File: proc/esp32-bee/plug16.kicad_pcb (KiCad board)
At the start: 2 copper layers, 37 x 31.6 mm, 17 parts, among them J7 Moat_Bus_device, Q5 2N7002, U1 VXO78, U3 P82B96, U4 P82B96, U5 ESPBEE

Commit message: Fixup espbee
move driver ICs away from the antenna
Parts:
- moved REF** 9.04 mm to (54.6, 50.8)
- moved C5 2.54 mm to (57.8, 52.9)
- moved C7 2.54 mm to (53.8, 52.9)
- moved U3 2.54 mm to (55.9, 48.9)
- moved U4 2.54 mm to (55.9, 56.9)
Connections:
- J7 pad 15: (no net) -> /TXD2
- J7 pad 17: (no net) -> /RXD2
- J7 pad 19: (no net) -> /T3
- U5 pad 13: (no net) -> Net-(U5-Pad13)
- U5 pad 8: (no net) -> Net-(U5-Pad8)
- U5 pad 9: (no net) -> Net-(U5-Pad9)
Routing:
- net /SDA: track 55.9 -> 47.4 mm
- net /BUS3: track 52.9 -> 49.4 mm
- net +24V: track 43.4 -> 40.5 mm
- net /BUS3_IN: track 48.6 -> 45.9 mm
- net /BUS4_IN: track 45.6 -> 43.0 mm
- net /SDA_IN: track 44.0 -> 41.4 mm
- net /SCL_IN: track 35.1 -> 32.7 mm
- net /EN: track 33.8 -> 35.9 mm
- net /Tx: track 45.1 -> 47.2 mm
- net /BUS4: track 41.4 -> 39.4 mm
- net GND: track 106.4 -> 104.7 mm, vias 8 -> 7
- net /SCL: track 43.3 -> 41.9 mm
- net /1w: track 17.1 -> 18.3 mm
- net +3V3: track 92.5 -> 91.6 mm
- net /Boot0: track 28.5 -> 29.3 mm
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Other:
- outline, holes or cut-outs redrawn
- board text added: "v2.1"
- board text removed: "V 1.2"

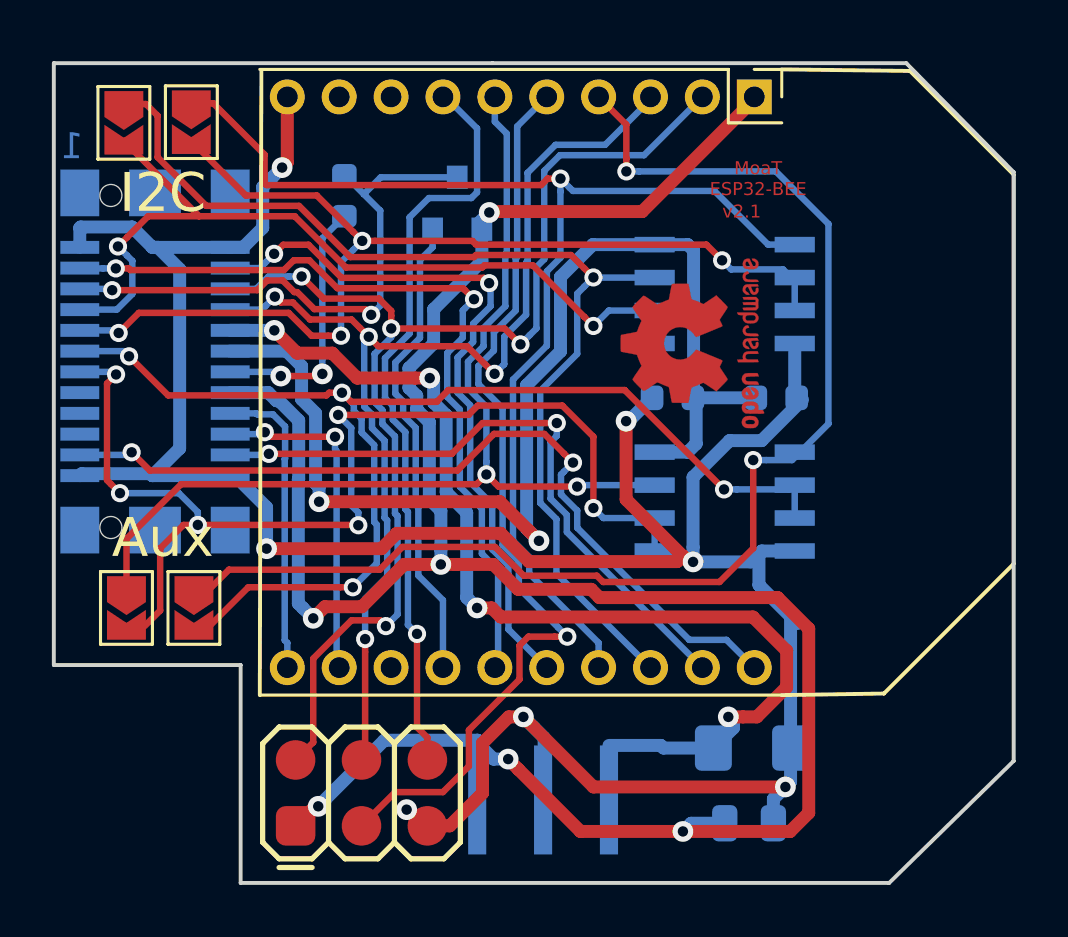
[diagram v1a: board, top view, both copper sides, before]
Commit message: Hierarchicalize proc
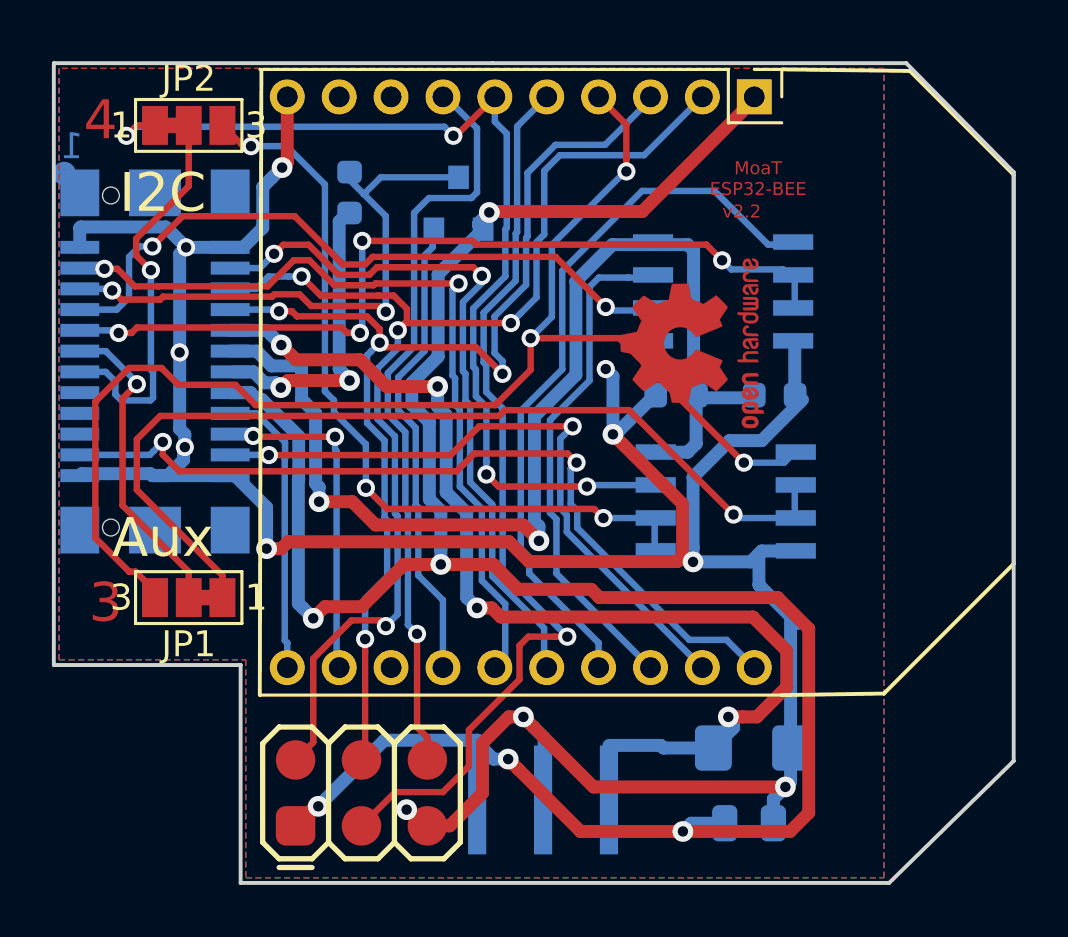
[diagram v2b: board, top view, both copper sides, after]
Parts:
- removed C5, C7: 100n, Capacitor_SMD:C_0603_1608Metric
- removed J7: Moat_Bus_device, localstuff:TE-1775013-2
- removed JP3, JP4: Jumper_NC, Jumper:SolderJumper-2_P1.3mm_Open_TrianglePad1.0x1.5mm
- removed Q5: 2N7002, Package_TO_SOT_SMD:SOT-23
- removed R4: 10k, Resistor_SMD:R_0603_1608Metric
- removed U4: P82B96, Package_SO:SOIC-8_3.9x4.9mm_P1.27mm
- added C1: 100n, Capacitor_SMD:C_0603_1608Metric, B.Cu at (57.8, 52.8)
- added C2: 100n, Capacitor_SMD:C_0603_1608Metric, B.Cu at (54.0, 52.8)
- added J1: Moat_Bus_device, localstuff:TE_1775013_plug, B.Cu at (33.9, 51.5)
- added Q1: 2N7002, Package_TO_SOT_SMD:SOT-23, B.Cu at (45.6, 45.4)
- added R1: 10k, Resistor_SMD:R_0603_1608Metric, B.Cu at (41.4, 45.0)
- added U2: P82B96, Package_SO:SOIC-8_3.9x4.9mm_P1.27mm, B.Cu at (55.8, 48.8)
- JP1, JP2: value Jumper_NC -> SolderJumper_3_Bridged12; footprint Jumper:SolderJumper-2_P1.3mm_Open_TrianglePad1.0x1.5mm -> Jumper:SolderJumper-3_P1.3mm_Bridged12_Pad1.0x1.5mm_NumberLabels
- moved JP1 18.3 mm to (35.2, 60.6), turned to 180 degrees
- moved U3 8.00 mm to (55.9, 56.9)
- moved JP2 2.50 mm to (35.2, 42.4), turned to 0 degrees
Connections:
- JP1 pad 1: /SDA -> Net-(JP1-Pad1)
- JP1 pad 2: /SDA_IN -> /Common bus interface/Bus3_12
- JP2 pad 1: /SCL -> /Bus4
- JP2 pad 2: /SCL_IN -> /Common bus interface/Bus4_12
- U3 pad 1: /SDA -> /Bus3
- U3 pad 2: /SDA_IN -> Net-(JP1-Pad1)
- U3 pad 3: /SDA_IN -> Net-(JP1-Pad1)
- U3 pad 5: /SCL_IN -> Net-(JP2-Pad3)
- U3 pad 6: /SCL_IN -> Net-(JP2-Pad3)
- U3 pad 7: /SCL -> /Bus4
- U5 pad 17: /SDA -> /Bus2
- U5 pad 18: /SCL -> /Bus1
- U5 pad 4: /BUS3 -> /Bus3
- U5 pad 6: /BUS4 -> /Bus4
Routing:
- net /Bus3: track 0.00 -> 52.0 mm, vias 0 -> 3
- net /BUS3: track 49.4 -> 0.00 mm, vias 2 -> 0
- net /SDA: track 47.4 -> 0.00 mm, vias 1 -> 0
- net /BUS3_IN: track 45.9 -> 0.00 mm, vias 4 -> 0
- net /BUS4_IN: track 43.0 -> 0.00 mm, vias 6 -> 0
- net /SCL: track 41.9 -> 0.00 mm, vias 1 -> 0
- net /SDA_IN: track 41.4 -> 0.00 mm, vias 4 -> 0
- net /BUS4: track 39.4 -> 0.00 mm, vias 2 -> 0
- net /Bus4: track 0.00 -> 38.7 mm, vias 0 -> 4
- net Net-(JP1-Pad1): track 0.00 -> 36.3 mm, vias 0 -> 1
- net /Common bus interface/Bus2_12: track 0.00 -> 33.0 mm, vias 0 -> 4
- net /SCL_IN: track 32.7 -> 0.00 mm, vias 2 -> 0
- net Net-(JP2-Pad3): track 0.00 -> 30.1 mm, vias 0 -> 3
- net /Bus2: track 0.00 -> 28.4 mm
- net /Common bus interface/Bus1_12: track 0.00 -> 27.6 mm, vias 0 -> 2
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- added copper zone on B.Cu, net GND
- added copper zone on F.Cu, net GND
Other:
- board text added: "3"
- board text added: "4"
- board text added: "v2.2"
- board text removed: "v2.1"

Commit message: esp module update
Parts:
- added C3: CP, Capacitor_SMD:C_0603_1608Metric, B.Cu at (56.0, 69.0)
- moved C6 14.0 mm to (43.1, 66.4), turned to 180 degrees
- moved JP1 2.24 mm to (33.0, 61.0)
- moved JP2 2.24 mm to (33.0, 42.0)
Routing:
- net /EN: track 35.7 -> 45.1 mm, vias 1 -> 2
- net GND: track 107.6 -> 112.8 mm
- net Net-(JP2-Pad3): track 30.1 -> 32.4 mm
- net /Bus4: track 38.7 -> 40.7 mm
- net /Bus3: track 52.0 -> 50.4 mm
- net /Bus2: track 28.4 -> 27.5 mm
- net /Rx: track 43.1 -> 42.4 mm
- net /Tx: track 46.6 -> 45.9 mm
- net +24V: track 40.5 -> 41.0 mm
- net /Common bus interface/Bus3_12: track 12.3 -> 11.8 mm
- net +3V3: track 91.2 -> 90.9 mm, vias 6 -> 5
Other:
- board text removed: "Aux"
- board text removed: "I2C"

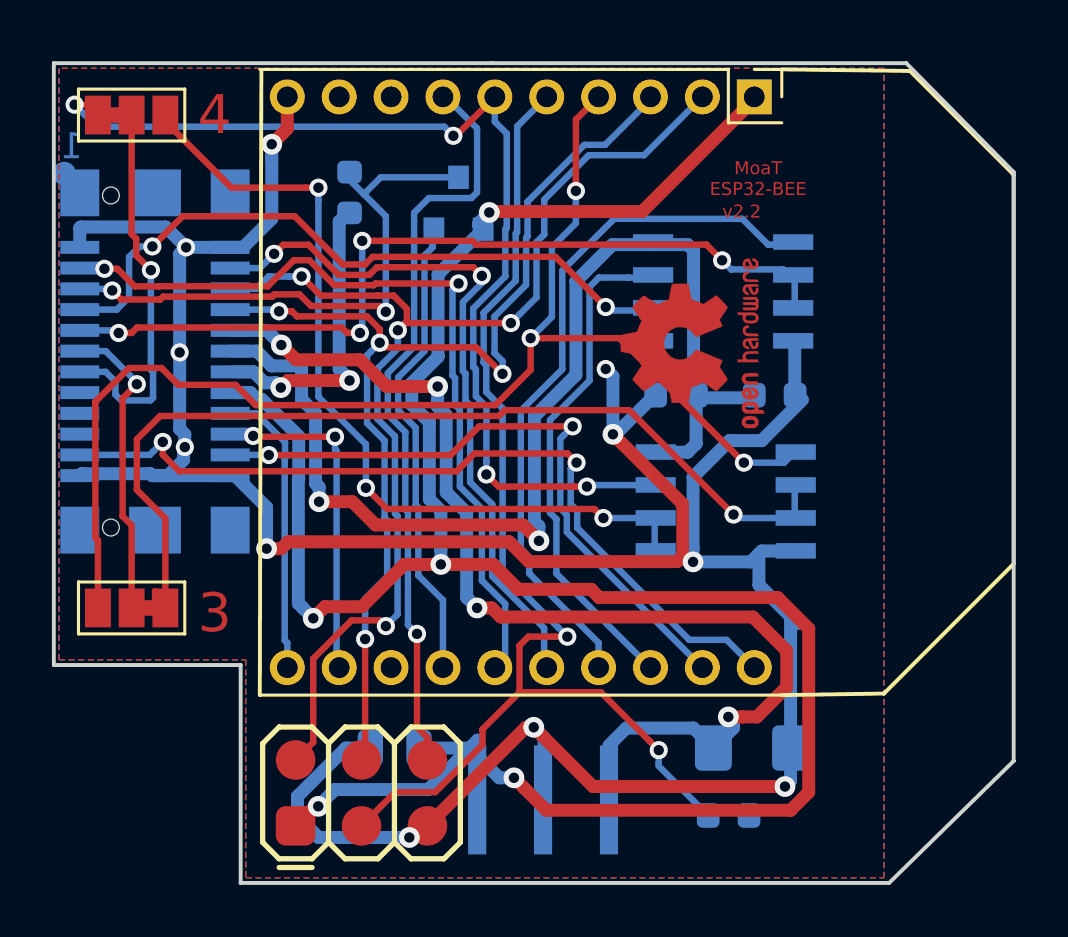
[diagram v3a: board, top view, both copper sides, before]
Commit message: Too many reworks to count.
Most notably: Split GND and GNDPWR.
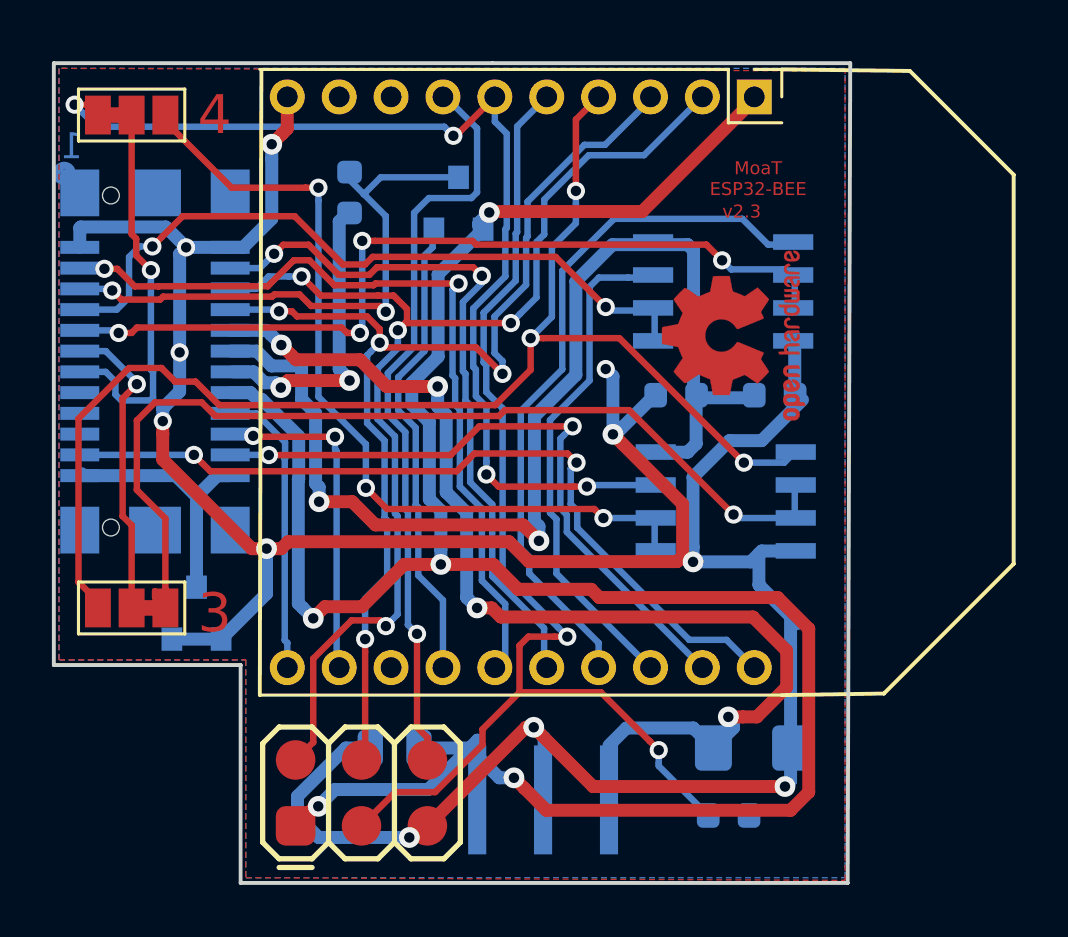
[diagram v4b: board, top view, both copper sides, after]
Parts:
- added D1: BAT54S, Package_TO_SOT_SMD:SOT-23, B.Cu at (35.5, 61.2)
- moved REF** 1.62 mm to (56.2, 50.5)
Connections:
- J1 pad 15: /Common bus interface/Tx2 -> (no net)
- J1 pad 17: /Common bus interface/Rx2 -> (no net)
- J1 pad 19: /Common bus interface/T3 -> (no net)
- J1 pad 23: GND -> GNDPWR
- J1 pad 24: GND -> GNDPWR
- U5 pad 13: Net-(U5-Pad13) -> (no net)
- U5 pad 8: Net-(U5-Pad8) -> (no net)
- U5 pad 9: Net-(U5-Pad9) -> (no net)
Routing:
- net GNDPWR: track 0.00 -> 10.1 mm
- net Net-(JP1-Pad1): track 36.0 -> 36.9 mm
- net GND: track 112.8 -> 113.6 mm
- net /T1: track 32.3 -> 31.6 mm
- net /Bus3: track 50.4 -> 50.9 mm
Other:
- board size 37 x 31.6 mm -> 30.7 x 31.6 mm
- board text added: "v2.3"
- board text removed: "v2.2"
